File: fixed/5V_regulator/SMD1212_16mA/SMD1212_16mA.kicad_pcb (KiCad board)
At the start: 2 copper layers, 25.4 x 20 mm, 18 parts, among them J1 Conn_01x04, J2 Conn_01x04, M1 MountingHole_2.5mm_Pad, M2 MountingHole_2.5mm_Pad, M3 MountingHole_2.5mm_Pad, M4 MountingHole_2.5mm_Pad, Q1 MMBT5551L, U1 TPS61222DCK, U2 LMV321

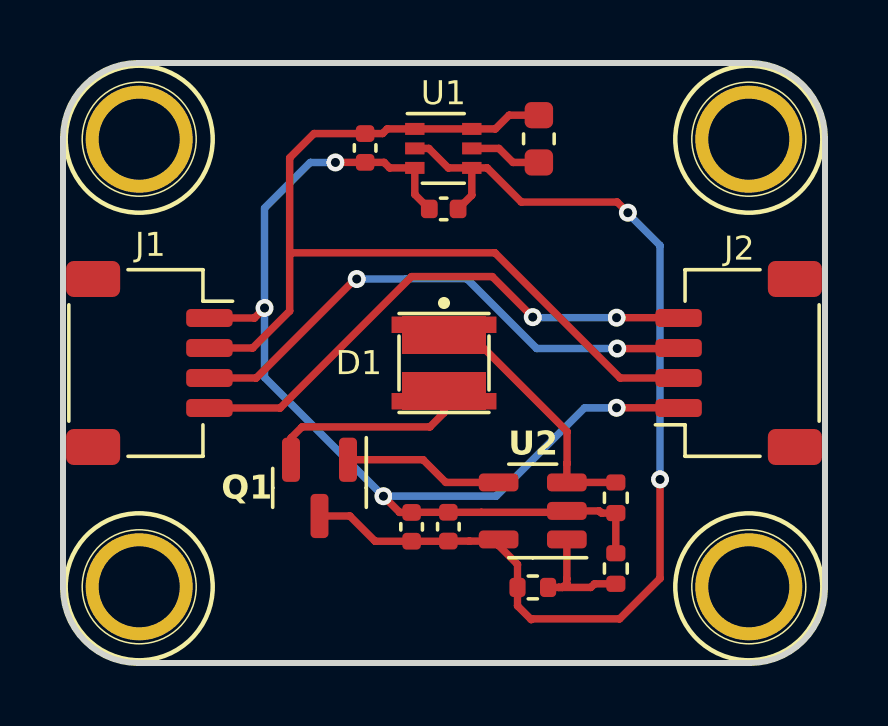
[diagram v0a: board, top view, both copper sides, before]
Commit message: Added part # to 'Symbol Fields Table" for SMD1212_16mA design.
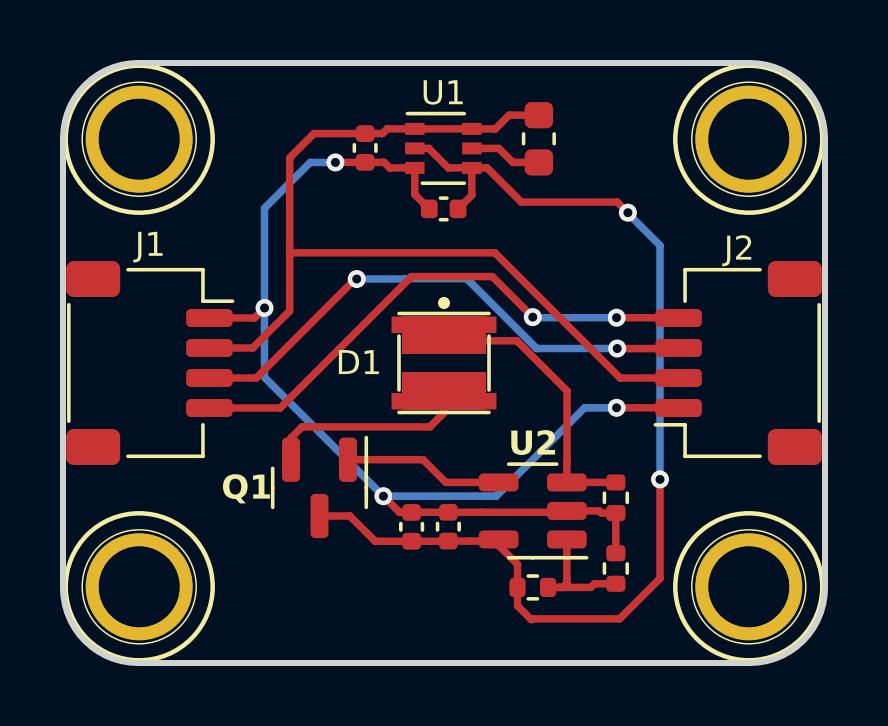
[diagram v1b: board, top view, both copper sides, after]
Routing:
- net Net-(D1-K): track 8.77 -> 10.8 mm
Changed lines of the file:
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@@
 	)
 	(gr_rect
-		(start 69.2023 55.5)
-		(end 74.7776 64.5)
+		(start 54.7 55.6)
+		(end 70.7 65)
 		(stroke
 			(width 0.12)
@@
 	)
 	(segment
+		(start 66.7952 63.981)
+		(end 66.7952 63.3544)
+		(width 0.25)
+		(layer "F.Cu")
+		(net 7)
+	)
+	(segment
 		(start 68.426 63.981)
 		(end 68.4276 63.9826)
@@
 	)
 	(segment
+		(start 63.985 59.075)
+		(end 62.7 59.075)
+		(width 0.25)
+		(layer "F.Cu")
+		(net 7)
+	)
+	(segment
+		(start 66.802 60.932)
+		(end 65.13 59.26)
+		(width 0.25)
+		(layer "F.Cu")
+		(net 7)
+	)
+	(segment
+		(start 63.825 59.075)
+		(end 62.7 59.075)
+		(width 0.25)
+		(layer "F.Cu")
+		(net 7)
+	)
+	(segment
+		(start 64.01 59.26)
+		(end 63.825 59.075)
+		(width 0.25)
+		(layer "F.Cu")
+		(net 7)
+	)
+	(segment
+		(start 66.7952 63.981)
+		(end 68.426 63.981)
+		(width 0.25)
+		(layer "F.Cu")
+		(net 7)
+	)
+	(segment
+		(start 66.802 63.3476)
+		(end 66.802 60.932)
+		(width 0.25)
+		(layer "F.Cu")
+		(net 7)
+	)
+	(segment
+		(start 65.13 59.26)
+		(end 64.01 59.26)
+		(width 0.25)
+		(layer "F.Cu")
+		(net 7)
+	)
+	(segment
 		(start 66.7952 63.3544)
 		(end 66.802 63.3476)
 		(width 0.25)
 		(layer "F.Cu")
-		(net 7)
-	)
-	(segment
-		(start 66.802 62.282)
-		(end 63.595 59.075)
-		(width 0.25)
-		(layer "F.Cu")
-		(net 7)
-	)
-	(segment
-		(start 66.802 63.3476)
-		(end 66.802 62.282)
-		(width 0.25)
-		(layer "F.Cu")
-		(net 7)
-	)
-	(segment
-		(start 66.7952 63.981)
-		(end 66.7952 63.3544)
-		(width 0.25)
-		(layer "F.Cu")
-		(net 7)
-	)
-	(segment
-		(start 63.595 59.075)
-		(end 62.7 59.075)
-		(width 0.25)
-		(layer "F.Cu")
-		(net 7)
-	)
-	(segment
-		(start 66.7952 63.981)
-		(end 68.426 63.981)
-		(width 0.25)
-		(layer "F.Cu")
